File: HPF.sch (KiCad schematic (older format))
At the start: 158 parts, among them J1 CONN_COAXIAL, J2 CONN_COAXIAL, J3 CONN_COAXIAL, J4 CONN_01X13, J5 CONN_COAXIAL, Q1 BSS84, U2 PGA103+

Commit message: firt routing, 6m LPF discarted
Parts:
- removed C5, C6: 10n, Capacitors_SMD:C_0805_HandSoldering, symbol C
- removed J2, J5: CONN_COAXIAL, SMA_PINS:SMA_PINS, symbol CONN_COAXIAL
- removed RL3: EC2-12 NU, 2_Form_C_Relay:THT_2_formC, symbol EE2-5NU
- C100, C101, C102, C103, C104, C105, C106, C107, C108, C109, C110, C111, C112, C113, C114, C115, C116, C117, C118, C119, C120, C121, C122, C123, C124, C125, C126, C127, C128, C129, C130, C131, C132, C133, C134, C135, C136, C137, C138, C139, C140, C141, C142, C143, C144, C145, C146, C147, C148, C149, C183, C89, C91, C92, C93, C94, C95, C96, C97, C98, C99: footprint Capacitors_SMD:C_0805_HandSoldering -> Capacitors_SMD:C_1206_HandSoldering
- J1, J3: footprint SMA_PINS:SMA_PINS -> Connectors:SMA_THT_Jack_Straight
- J4: footprint conn_kk100:kk100_22-23-2131 -> Connectors:IDC_Header_Straight_14pins
- L17, L18, L19, L20, L21, L22, L23, L24, L25, L26, L27, L28, L29, L30, L31, L32, L33: footprint T50_V_cms:T50_V_smd -> T50:T50_V_THT
- Q1: symbol IRF9540N -> IRF9540N-RESCUE-HPF
- RL1, RL16, RL17, RL18, RL19, RL2, RL20, RL21, RL22, RL23, RL24, RL25, RL26, RL27, RL28, RL29: footprint 2_Form_C_Relay:THT_2_formC -> 2_Form_C_Relay:Relay_DPDT_NEC_EC2
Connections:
- wire segments 405 -> 386
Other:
- note added: "All relays \nKemet/NEC/Tokin\nEC2-12 NU\n12V non latching\nTHT"
- note added: "GBLC03C\nou \néquivalent"
- note added: "HPF \nOut"
- note added: "from lpf 60MHz/\nPS-RX switch"
- note removed: "All relays \nKemet/NEC/Tokin\nEC2-12 NU\n12V non latching\nthru cnx"
- note removed: "All relays \nKemet/NEC/Tokin\nEC2-12 NU\n5V non latching\ngull wing"
- note removed: "Out"
- note removed: "To PS_Feedback\nps/SWR Board"
- note removed: "To RX Bypass\nRelay\n"
- moved on the sheet: C1, C2, C3, C4, D2, D3, D4, D5, J3, R1, R10, R11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

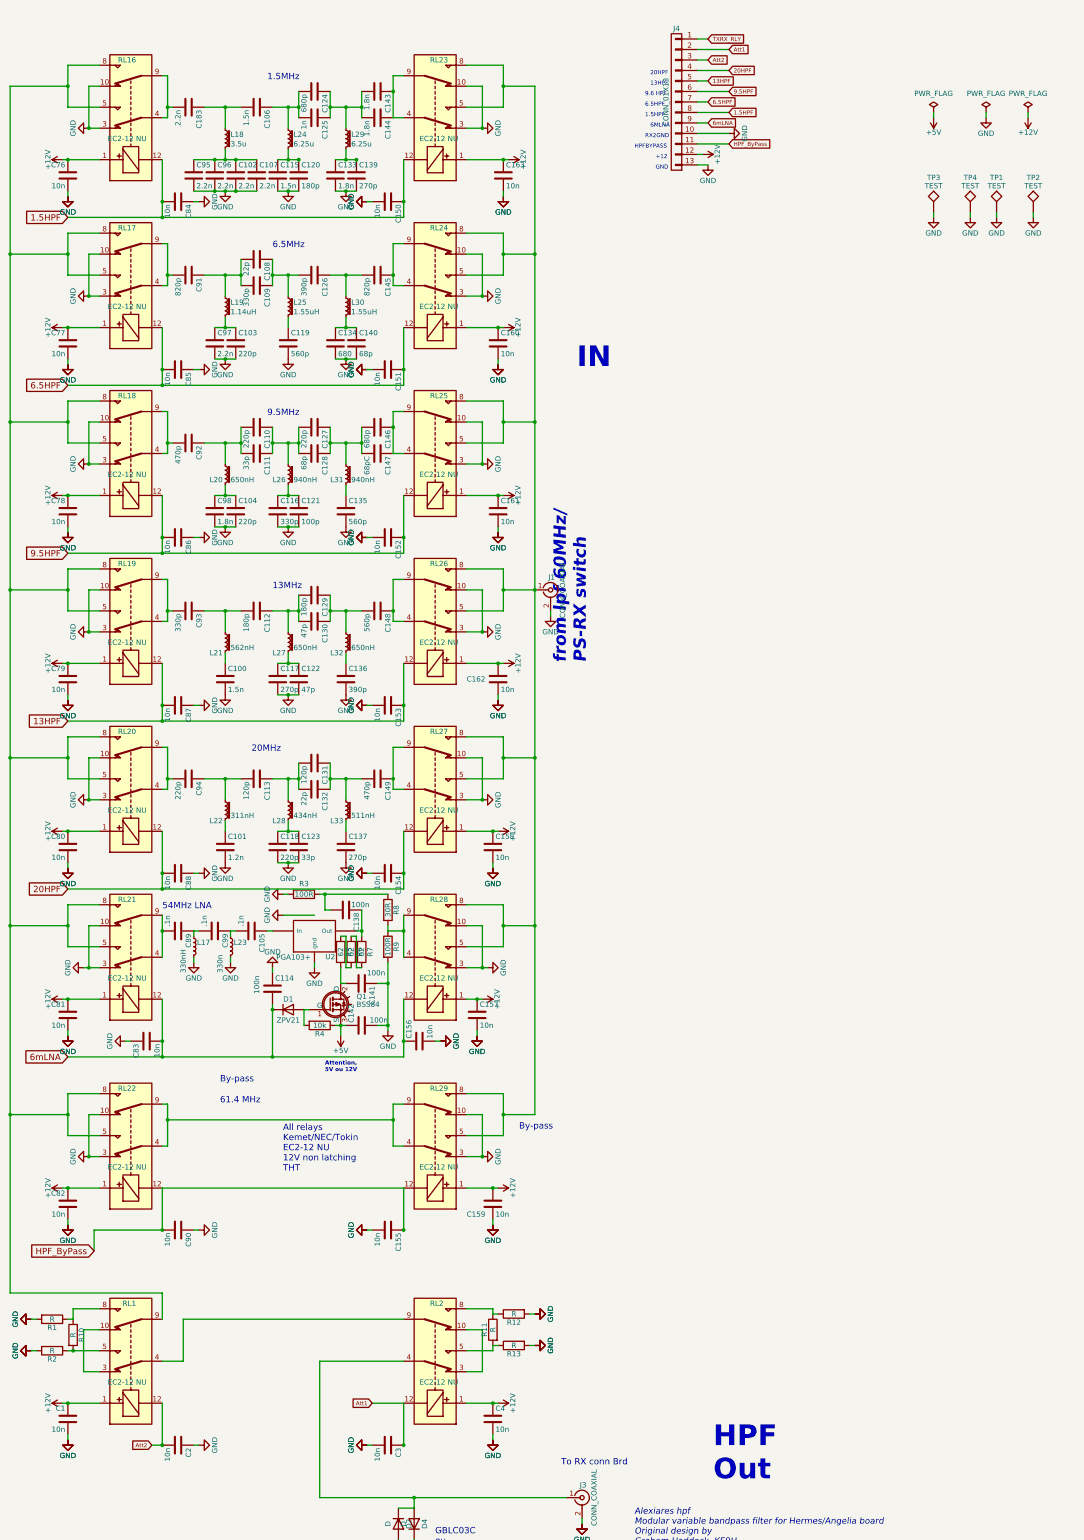
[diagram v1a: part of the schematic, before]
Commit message: silkmask cleanup and comments added
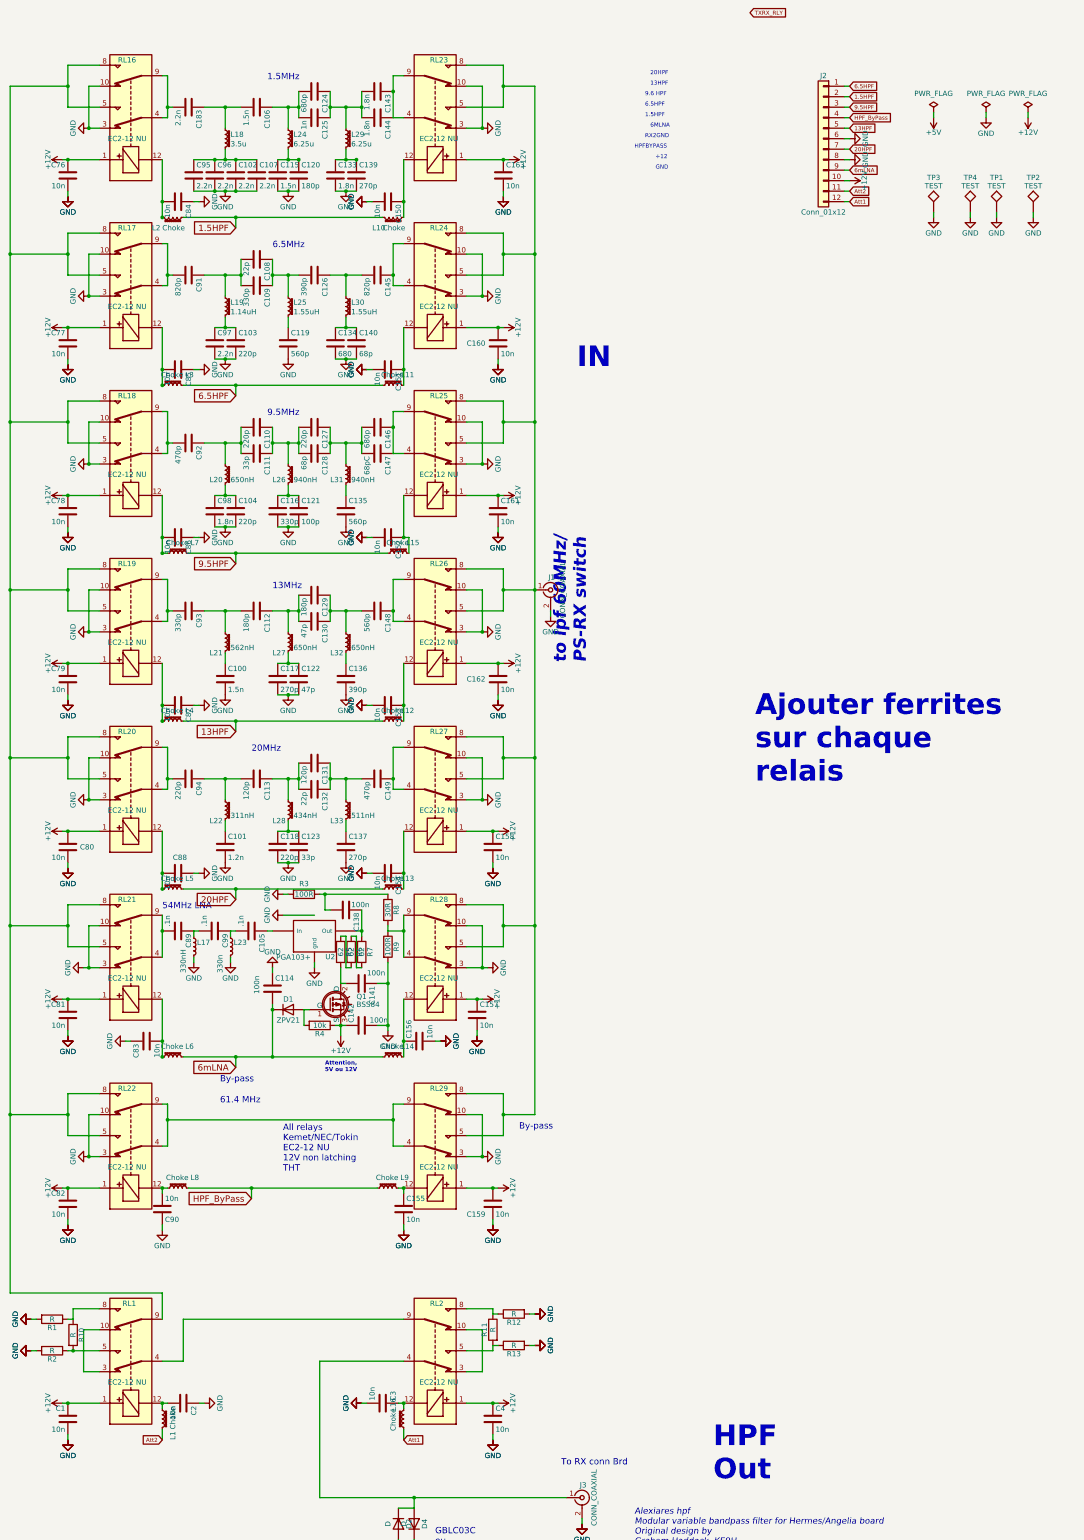
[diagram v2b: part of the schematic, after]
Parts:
- removed J4: CONN_01X13, Connectors:IDC_Header_Straight_14pins, symbol CONN_01X13
- added J2: Conn_01x12, Connect:IDC_Header_Straight_12pins, symbol Conn_01x12
- added L1, L10, L11, L12, L13, L14, L15, L16, L2, L3, L4, L5, L6, L7, L8, L9: Choke, Inductors_SMD:L_0805_HandSoldering, symbol L_Core_Ferrite_Small
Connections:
- net +12V: now also C142.1, Q1.3 (S), R4.1, J2.10 (Pin_10)
- net +5V: no longer C142.1, Q1.3 (S), R4.1
- net 1.5HPF: now also J2.2 (Pin_2), L10.2, L2.1; no longer C150.1, C84.2, RL16.12, RL23.12
- net 13HPF: now also J2.5 (Pin_5), L12.1, L4.2; no longer C153.1, C87.2, RL19.12, RL26.12
- net 20HPF: now also J2.7 (Pin_7), L13.1, L5.2; no longer C154.1, C88.2, RL20.12, RL27.12
- net 6.5HPF: now also J2.1 (Pin_1), L11.1, L3.2; no longer C151.1, C85.2, RL17.12, RL24.12
- net 6mLNA: now also J2.9 (Pin_9), L14.1, L6.2; no longer C156.1, C83.2, RL21.12, RL28.12
- net 9.5HPF: now also J2.3 (Pin_3), L15.1, L7.2; no longer C152.1, C86.2, RL18.12, RL25.12
- net Att1: now also J2.12 (Pin_12), L16.1; no longer C3.1, RL2.12
- net Att2: now also J2.11 (Pin_11), L1.2; no longer C2.2, RL1.12
- net GND: now also J2.6 (Pin_6), J2.8 (Pin_8)
- net HPF_ByPass: now also J2.4 (Pin_4), L8.2, L9.1; no longer C155.1, C90.2, RL22.12, RL29.12
- new net: C84.2, L2.2, RL16.12
- new net: C150.1, L10.1, RL23.12
- new net: C85.2, L3.1, RL17.12
- new net: C151.1, L11.2, RL24.12
- new net: C86.2, L7.1, RL18.12
- new net: C152.1, L15.2, RL25.12
- new net: C87.2, L4.1, RL19.12
- new net: C153.1, L12.2, RL26.12
- new net: C88.2, L5.1, RL20.12
- new net: C154.1, L13.2, RL27.12
- new net: C90.2, L8.1, RL22.12
- new net: C155.1, L9.2, RL29.12
- new net: C83.2, L6.1, RL21.12
- new net: C156.1, L14.2, RL28.12
- new net: C3.1, L16.2, RL2.12
- new net: C2.2, L1.1, RL1.12
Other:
- note added: "Ajouter ferrites \nsur chaque \nrelais"
- note added: "to lpf 60MHz/\nPS-RX switch"
- note removed: "from lpf 60MHz/\nPS-RX switch"
- moved on the sheet: C155, C2, C3, C90

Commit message: New LNA, silkmask modified
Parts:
- removed C105, C89, C99: .1n, Capacitors_SMD:C_1206_HandSoldering, symbol C
- removed C114, C138, C141, C142: 100n, Capacitors_SMD:C_1206_HandSoldering, symbol C
- removed Q1: BSS84, TO_SOT_Packages_SMD:SOT-23_Handsoldering, symbol IRF9540N-RESCUE-HPF
- removed R3, R9: 100R, Resistors_SMD:R_0805_HandSoldering, symbol R
- removed R4: 10k, Resistors_SMD:R_0805_HandSoldering, symbol R
- removed R5, R6, R7: 62, Resistors_SMD:R_0805_HandSoldering, symbol R
- removed R8: 30R, Resistors_SMD:R_0805_HandSoldering, symbol R
- added C10, C13, C16: 100p, Capacitors_SMD:C_0805_HandSoldering, symbol C_Small
- added C11: 10p, Capacitors_SMD:C_0805_HandSoldering, symbol C_Small
- added C12, C15: 60p, Capacitors_SMD:C_0805_HandSoldering, symbol C_Small
- added C14, C9: 10uf, Capacitors_Tantalum_SMD:CP_Tantalum_Case-B_EIA-3528-21_Hand, symbol C_Small
- added C5, C6: 10n, Capacitors_SMD:C_0805_HandSoldering, symbol C_Small
- added C7: 100n, Capacitors_SMD:C_0805_HandSoldering, symbol C_Small
- added C8: 1n, Capacitors_SMD:C_0805_HandSoldering, symbol C_Small
- added L34, L35: 220n, Inductors_SMD:L_0805_HandSoldering, symbol L_Small
- added Q2: zvp2106G, TO_SOT_Packages_SMD:SOT-23_Handsoldering, symbol IRF9540N-RESCUE-HPF
- added R3: 18, Resistors_SMD:R_0805_HandSoldering, symbol R_Small
- added R5: 10k, Resistors_SMD:R_0805_HandSoldering, symbol R_Small
- added U1: AP1117-50, TO_SOT_Packages_SMD:SOT-223-3_TabPin2, symbol AP1117-50
- D1: value ZPV21 -> diode
- L17: value 330nH -> 220n; footprint T50:T50_V_THT -> Inductors_SMD:L_0805_HandSoldering
- L23: value 330n -> 220n; footprint T50:T50_V_THT -> Inductors_SMD:L_0805_HandSoldering
- U2: footprint (none) -> TO_SOT_Packages_SMD:SOT-89-3_Handsoldering
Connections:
- net +12V: now also C11.2, C13.2, C14.2, U1.3 (VI)
- net GND: now also C11.1, C13.1, C14.1, C6.2, C7.2, C8.2, C9.1, L34.2, L35.2, U1.1 (GND); no longer L17.2
- net at L17.1: now also U2.3 (Out), C5.1
- net at RL21.4, RL21.9: now also C5.2
- net at L23.1: now also C10.1, C12.2
- net at U2.1 (In): now also C10.2
- net at D1.2 (A): now also Q2.1 (G), R5.2
- net at RL28.4, RL28.9: now also C16.1
- new net: C12.1, C15.2, L34.1
- new net: C15.1, C16.2, L35.1
- new net: L17.2, R3.1
- new net: C6.1, C7.1, C8.1, Q2.2 (D), R3.2
- new net: C9.2, Q2.3 (S), R5.1, U1.2 (VO)
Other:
- note added: "HPF\nIN"
- note added: "ZVP2106G\nrs-275-967"
- note removed: "Ajouter ferrites \nsur chaque \nrelais"
- note removed: "Attention, \n5V ou 12V"
- note removed: "IN"
- moved on the sheet: C156, C83, D1, L14, L6, U2

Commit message: edge SMA added, main connector shifted
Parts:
- added J4, J5: CONN_COAXIAL, Connector_Coaxial:SMA_Amphenol_132289_EdgeMount, symbol CONN_COAXIAL
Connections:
- net GND: now also J4.2 (Ext), J5.2 (Ext)
- net at J1.1 (In), RL23.5, RL23.8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: now also J4.1 (In)
- net at D2.1 (K), D4.2 (A), J3.1 (In)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: now also J5.1 (In)
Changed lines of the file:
@@
 Wire Wire Line
 	4600 9350 4850 9350
+$Comp
+L CONN_COAXIAL J5
+U 1 1 5A2FBABA
+P 6250 14950
+F 0 "J5" H 6260 15070 50  0000 C CNN
+F 1 "CONN_COAXIAL" V 6365 14950 50  0000 C CNN
+F 2 "Connector_Coaxial:SMA_Amphenol_132289_EdgeMount" H 6250 14950 50  0001 C CNN
+F 3 "" H 6250 14950 50  0001 C CNN
+	1    6250 14950
+	1    0    0    -1
+$EndComp
+Wire Wire Line
+	6250 15150 6250 15200
+$Comp
+L GND #PWR0141
+U 1 1 5A2FBAC1
+P 6250 15200
+F 0 "#PWR0141" H 6250 14950 50  0001 C CNN
+F 1 "GND" H 6250 15050 50  0000 C CNN
+F 2 "" H 6250 15200 50  0000 C CNN
+F 3 "" H 6250 15200 50  0000 C CNN
+	1    6250 15200
+	1    0    0    -1
+$EndComp
+$Comp
+L GND #PWR0142
+U 1 1 5A2FBAC7
+P 6250 15200
+F 0 "#PWR0142" H 6250 14950 50  0001 C CNN
+F 1 "GND" H 6250 15050 50  0000 C CNN
+F 2 "" H 6250 15200 50  0000 C CNN
+F 3 "" H 6250 15200 50  0000 C CNN
+	1    6250 15200
+	1    0    0    -1
+$EndComp
+Wire Wire Line
+	6100 14950 6100 14750
+Connection ~ 6100 14750
+Wire Wire Line
+	6250 6900 6250 6950
+$Comp
+L GND #PWR0143
+U 1 1 5A2FC743
+P 6250 6950
+F 0 "#PWR0143" H 6250 6700 50  0001 C CNN
+F 1 "GND" H 6250 6800 50  0000 C CNN
+F 2 "" H 6250 6950 50  0000 C CNN
+F 3 "" H 6250 6950 50  0000 C CNN
+	1    6250 6950
+	-1   0    0    -1
+$EndComp
+$Comp
+L CONN_COAXIAL J4
+U 1 1 5A2FC749
+P 6250 6700
+F 0 "J4" H 6260 6820 50  0000 C CNN
+F 1 "CONN_COAXIAL" V 6365 6700 50  0000 C CNN
+F 2 "Connector_Coaxial:SMA_Amphenol_132289_EdgeMount" H 6250 6700 50  0001 C CNN
+F 3 "" H 6250 6700 50  0001 C CNN
+	1    6250 6700
+	1    0    0    -1
+$EndComp
+Connection ~ 6100 6700
 $EndSCHEMATC

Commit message: changed sma footprint, gerber done
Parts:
- J4, J5: footprint Connector_Coaxial:SMA_Amphenol_132289_EdgeMount -> SMA_PINS:SMA_EDGE_NRW
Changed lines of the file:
@@
 F 0 "J5" H 6260 15070 50  0000 C CNN
 F 1 "CONN_COAXIAL" V 6365 14950 50  0000 C CNN
-F 2 "Connector_Coaxial:SMA_Amphenol_132289_EdgeMount" H 6250 14950 50  0001 C CNN
+F 2 "SMA_PINS:SMA_EDGE_NRW" H 6250 14950 50  0001 C CNN
 F 3 "" H 6250 14950 50  0001 C CNN
 	1    6250 14950
@@
 F 0 "J4" H 6260 6820 50  0000 C CNN
 F 1 "CONN_COAXIAL" V 6365 6700 50  0000 C CNN
-F 2 "Connector_Coaxial:SMA_Amphenol_132289_EdgeMount" H 6250 6700 50  0001 C CNN
+F 2 "SMA_PINS:SMA_EDGE_NRW" H 6250 6700 50  0001 C CNN
 F 3 "" H 6250 6700 50  0001 C CNN
 	1    6250 6700

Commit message: new stitching, new gerber
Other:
- note added: "HPF \nIN"
- note added: "HPF\nout\n"
- note added: "To RX Coax Out\n"
- note removed: "HPF \nOut"
- note removed: "HPF\nIN"
- note removed: "To RX conn Brd\n"
- note removed: "to lpf 60MHz/\nPS-RX switch"
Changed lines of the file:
@@
 Connection ~ 1100 9300
 Text Notes 7350 14550 0    197  ~ 39
-HPF \nOut
+HPF \nIN
 Text Notes 6550 5250 0    197  ~ 39
-HPF\nIN
+HPF\nout\n
 Wire Wire Line
 	1100 1300 1100 12800
@@
 $EndComp
 Text Notes 6350 14450 0    60   ~ 0
-To RX conn Brd\n
+To RX Coax Out\n
 $Comp
 L +12V #PWR0111
@@
 	1    0    0    -1
 $EndComp
-Text Notes 7100 6650 1    118  Italic 24
-to lpf 60MHz/\nPS-RX switch
 Wire Wire Line
 	6100 6100 5800 6100

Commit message: BOM added, new Gerber
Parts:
- C134: value 680 -> 680p
- R1, R2: value R -> 100R
- R10: value R -> 75R
- R11: value R -> 240R
- R12, R13: value R -> 62R
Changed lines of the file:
@@
 P 4200 3750
 F 0 "C134" H 4225 3850 50  0000 L CNN
-F 1 "680" H 4225 3650 50  0000 L CNN
+F 1 "680p" H 4225 3650 50  0000 L CNN
 F 2 "Capacitors_SMD:C_1206_HandSoldering" H 4238 3600 50  0001 C CNN
 F 3 "" H 4200 3750 50  0000 C CNN
@@
 P 1700 13200
 F 0 "R10" V 1780 13200 50  0000 C CNN
-F 1 "R" V 1700 13200 50  0000 C CNN
+F 1 "75R" V 1700 13200 50  0000 C CNN
 F 2 "Resistors_SMD:R_0805_HandSoldering" V 1630 13200 50  0001 C CNN
 F 3 "" H 1700 13200 50  0001 C CNN
@@
 P 1500 13050
 F 0 "R1" V 1580 13050 50  0000 C CNN
-F 1 "R" V 1500 13050 50  0000 C CNN
+F 1 "100R" V 1500 13050 50  0000 C CNN
 F 2 "Resistors_SMD:R_0805_HandSoldering" V 1430 13050 50  0001 C CNN
 F 3 "" H 1500 13050 50  0001 C CNN
@@
 P 1500 13350
 F 0 "R2" V 1580 13350 50  0000 C CNN
-F 1 "R" V 1500 13350 50  0000 C CNN
+F 1 "100R" V 1500 13350 50  0000 C CNN
 F 2 "Resistors_SMD:R_0805_HandSoldering" V 1430 13350 50  0001 C CNN
 F 3 "" H 1500 13350 50  0001 C CNN
@@
 P 5700 13150
 F 0 "R11" V 5780 13150 50  0000 C CNN
-F 1 "R" V 5700 13150 50  0000 C CNN
+F 1 "240R" V 5700 13150 50  0000 C CNN
 F 2 "Resistors_SMD:R_0805_HandSoldering" V 5630 13150 50  0001 C CNN
 F 3 "" H 5700 13150 50  0001 C CNN
@@
 P 5900 13000
 F 0 "R12" V 5980 13000 50  0000 C CNN
-F 1 "R" V 5900 13000 50  0000 C CNN
+F 1 "62R" V 5900 13000 50  0000 C CNN
 F 2 "Resistors_SMD:R_0805_HandSoldering" V 5830 13000 50  0001 C CNN
 F 3 "" H 5900 13000 50  0001 C CNN
@@
 P 5900 13300
 F 0 "R13" V 5980 13300 50  0000 C CNN
-F 1 "R" V 5900 13300 50  0000 C CNN
+F 1 "62R" V 5900 13300 50  0000 C CNN
 F 2 "Resistors_SMD:R_0805_HandSoldering" V 5830 13300 50  0001 C CNN
 F 3 "" H 5900 13300 50  0001 C CNN

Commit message: silkmask mods,, gnd stitching cleaning, gerber added
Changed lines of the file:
@@
 	0    1    1    0
 $EndComp
-Text Notes 7200 1200 0    39   ~ 0
+Text Notes 7100 1250 0    39   ~ 0
 20HPF\n
-Text Notes 7200 1300 0    39   ~ 0
+Text Notes 7100 1350 0    39   ~ 0
 13HPF\n
-Text Notes 7150 1400 0    39   ~ 0
+Text Notes 7050 1450 0    39   ~ 0
 9.6 HPF\n
-Text Notes 7150 1500 0    39   ~ 0
+Text Notes 7050 1550 0    39   ~ 0
 6.5HPF\n
-Text Notes 7150 1600 0    39   ~ 0
+Text Notes 7050 1650 0    39   ~ 0
 1.5HPF\n
-Text Notes 7200 1700 0    39   ~ 0
+Text Notes 7100 1750 0    39   ~ 0
 6MLNA
-Text Notes 7150 1800 0    39   ~ 0
+Text Notes 7050 1850 0    39   ~ 0
 RX2GND\n
-Text Notes 7050 1900 0    39   ~ 0
+Text Notes 6950 1950 0    39   ~ 0
 HPFBYPASS\n
-Text Notes 7250 2000 0    39   ~ 0
+Text Notes 7150 2050 0    39   ~ 0
 +12\n
-Text Notes 7250 2100 0    39   ~ 0
+Text Notes 7150 2150 0    39   ~ 0
 GND\n
 Text GLabel 9100 1400 2    39   Input ~ 0
